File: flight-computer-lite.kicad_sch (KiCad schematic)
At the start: 23 parts, among them J1 USB_C_Receptacle_USB2.0_16P, J2 Micro_SD_Card_Det2, J3 Conn_01x02_Pin, J4 Conn_01x02_Pin, Q1 BSS138, U1 RP2040, U2 W25Q32JVZP, Y1 SiT1602BI-22-33E-12.000000E

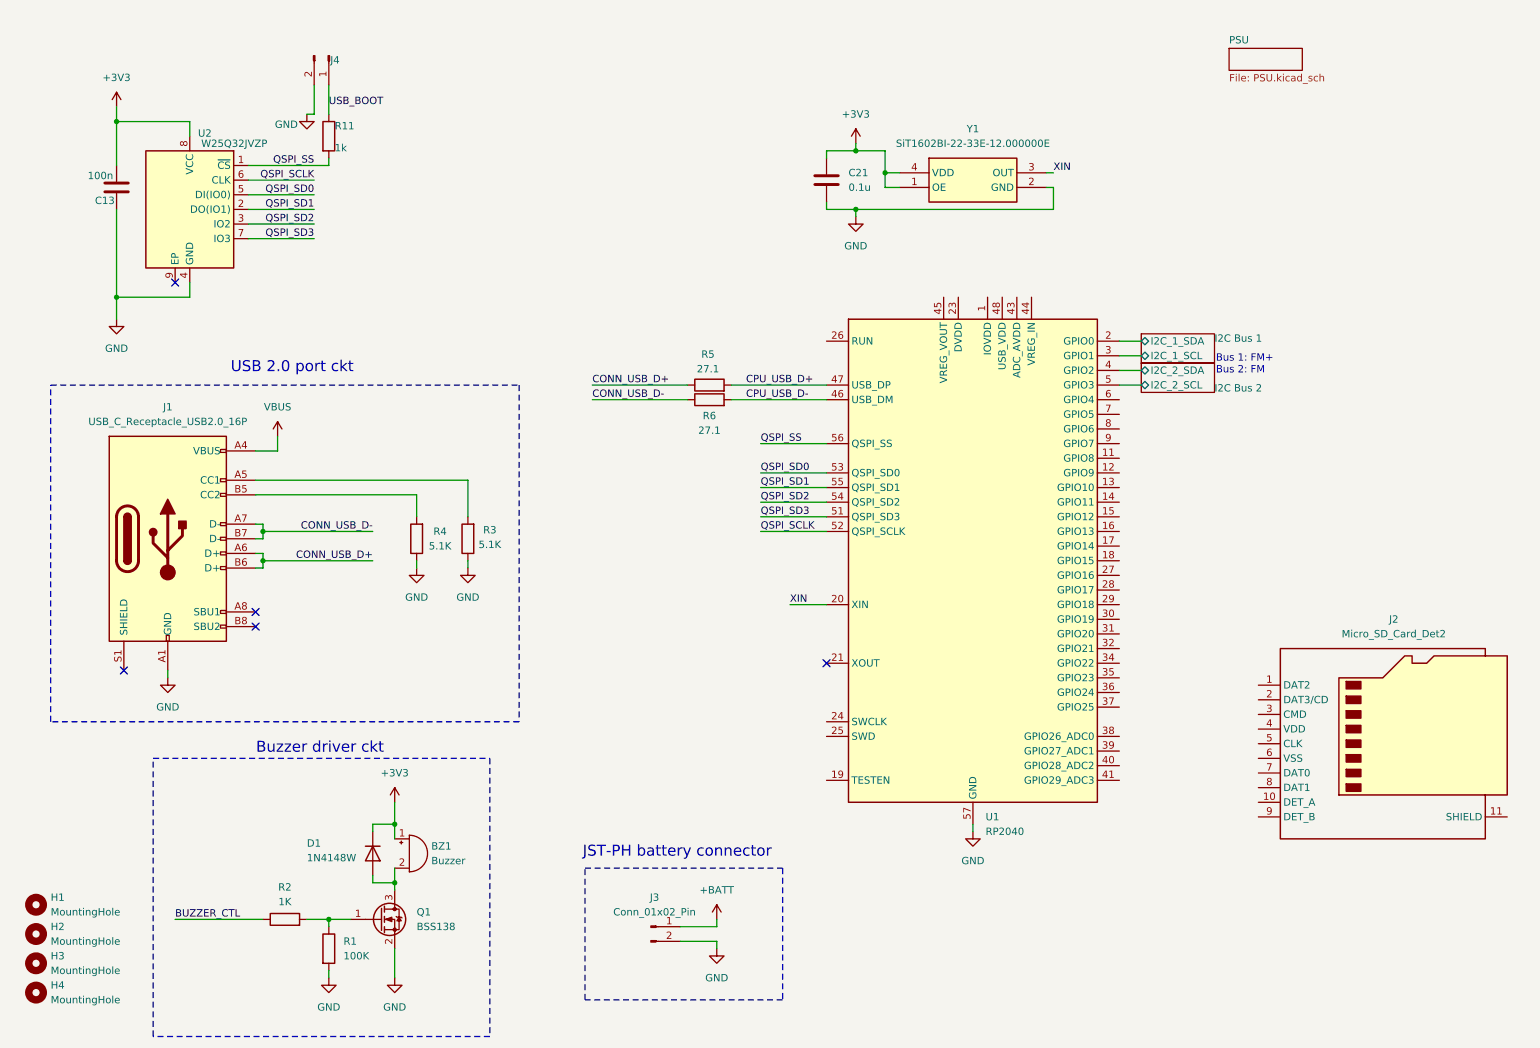
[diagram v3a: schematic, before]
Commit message: Added buttons, LEDs, TPs, and Miku
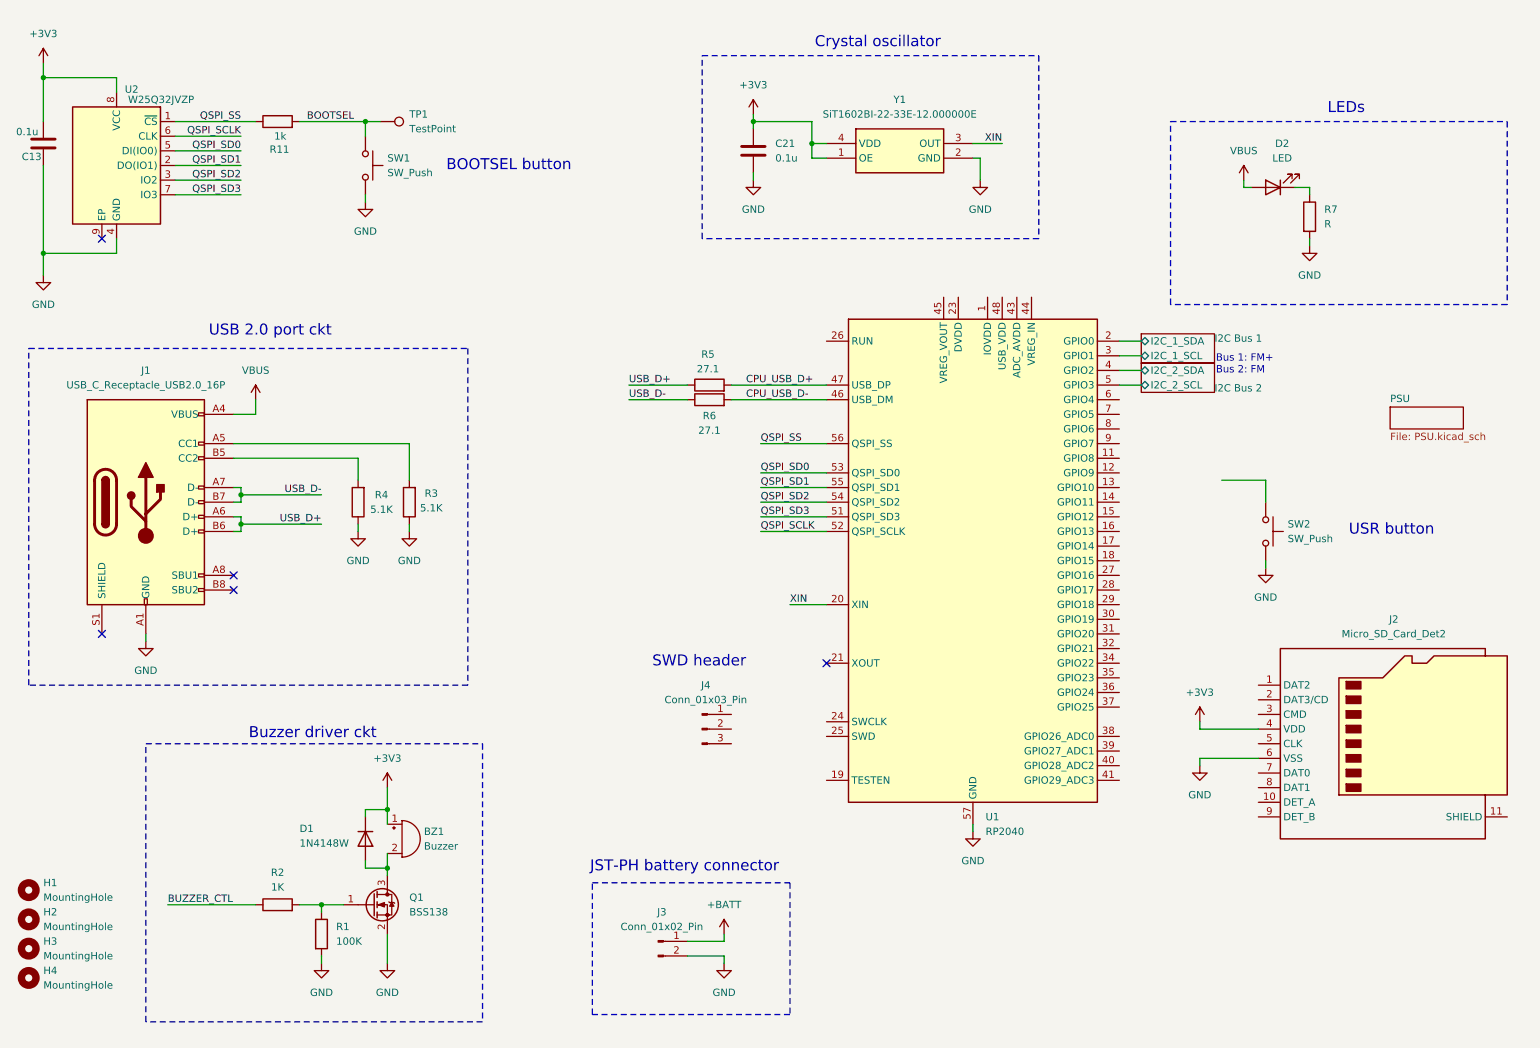
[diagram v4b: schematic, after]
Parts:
- removed J4: Conn_01x02_Pin, Connector_JST:JST_PH_S2B-PH-SM4-TB_1x02-1MP_P2.00mm_Horizontal, symbol Connector:Conn_01x02_Pin
- added D2: LED, LED_SMD:LED_0603_1608Metric, symbol Device:LED
- added J4: Conn_01x03_Pin, Connector_JST:JST_PH_B3B-PH-K_1x03_P2.00mm_Vertical, symbol Connector:Conn_01x03_Pin
- added R7: R, Resistor_SMD:R_0603_1608Metric, symbol Device:R
- added SW1, SW2: SW_Push, Button_Switch_SMD:SW_Push_1P1T_NO_Vertical_Wuerth_434133025816, symbol Switch:SW_Push
- added TP1: TestPoint, TestPoint:TestPoint_Pad_D1.0mm, symbol Connector:TestPoint
- C13: value 100n -> 0.1u
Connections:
- net USB_BOOT is gone; now on net QSPI_SS: R11.1
- net +3V3: now also J2.4 (VDD)
- net GND: now also J2.6 (VSS), R7.2, SW1.2, SW2.2
- net QSPI_SS: no longer R11.2
- net VBUS: now also D2.2 (A)
- net CONN_USB_D+ renamed USB_D+
- net CONN_USB_D- renamed USB_D-
- new net: D2.1 (K), R7.1
- new net BOOTSEL: R11.2, SW1.1, TP1.1
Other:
- note added: "BOOTSEL button"
- note added: "Crystal oscillator"
- note added: "LEDs"
- note added: "SWD header"
- note added: "USR button"
- moved on the sheet: BZ1, C13, C21, D1, H1, H2, H3, H4, J1, J3, Q1, R1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

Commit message: Added more decoupling caps
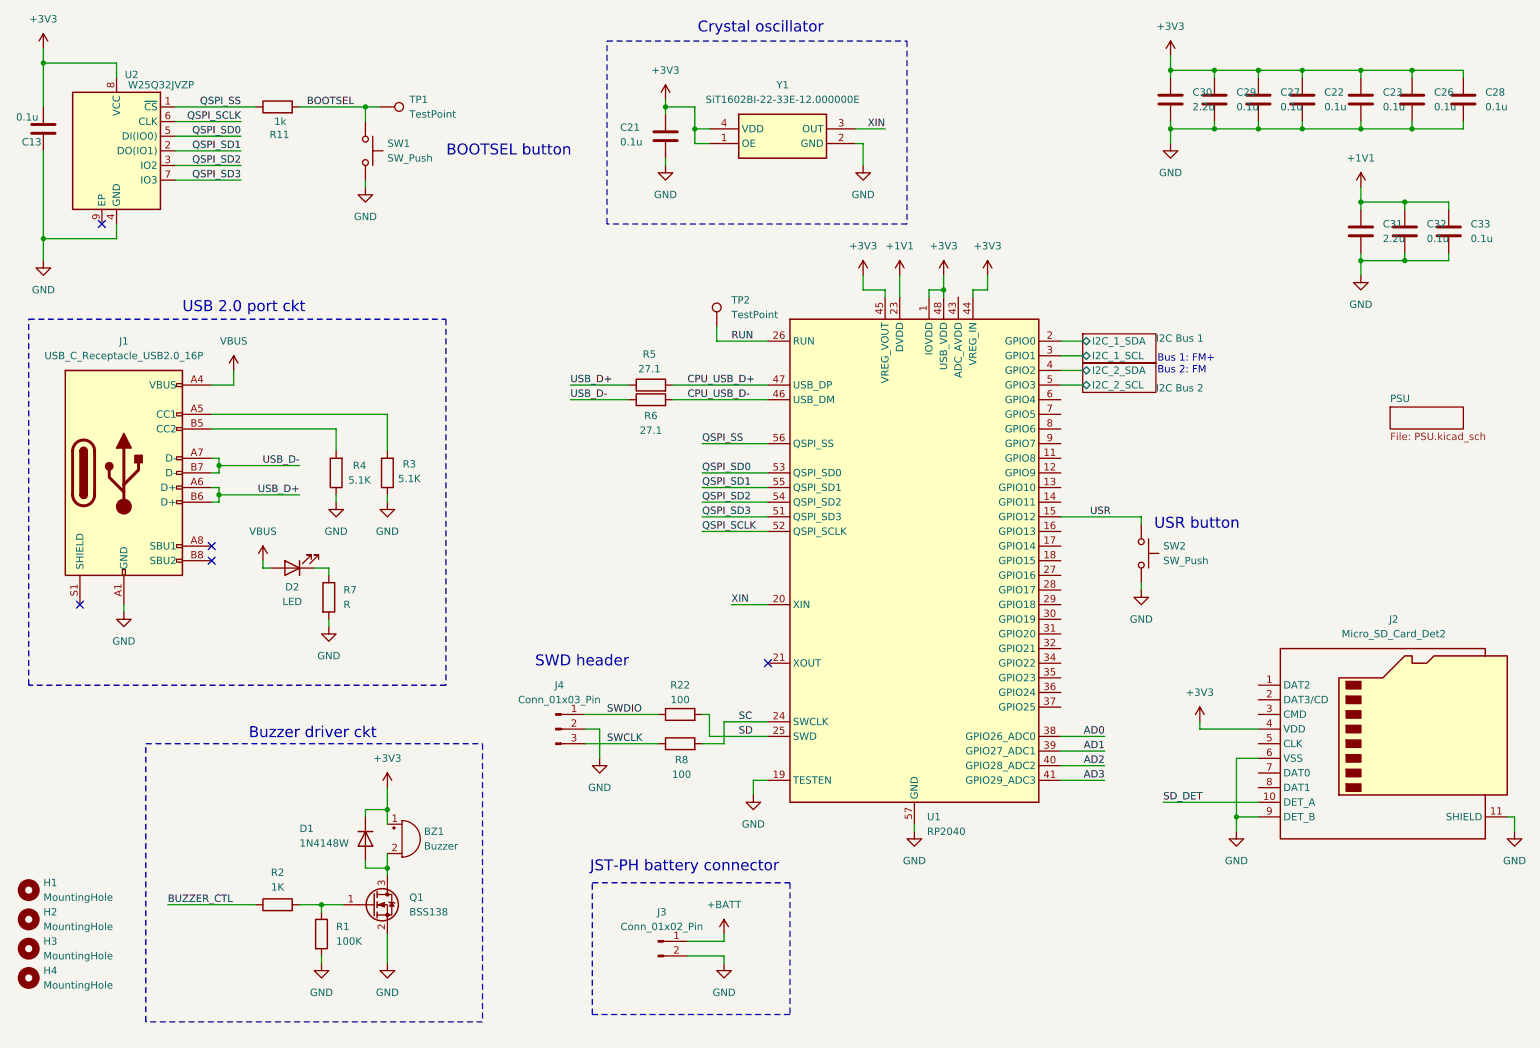
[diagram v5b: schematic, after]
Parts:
- added C22, C23, C26, C27, C28, C29, C32, C33: 0.1u, Capacitor_SMD:C_0603_1608Metric, symbol Device:C
- added C30, C31: 2.2u, Capacitor_SMD:C_0603_1608Metric, symbol Device:C
- added R22, R8: 100, Resistor_SMD:R_0603_1608Metric, symbol Device:R
- added TP2: TestPoint, TestPoint:TestPoint_Pad_D1.0mm, symbol Connector:TestPoint
- J4: footprint Connector_JST:JST_PH_B3B-PH-K_1x03_P2.00mm_Vertical -> Connector_JST:JST_SH_BM03B-SRSS-TB_1x03-1MP_P1.00mm_Vertical
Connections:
- net +3V3: now also U1.1 (IOVDD), U1.10 (IOVDD), U1.22 (IOVDD), U1.33 (IOVDD), U1.42 (IOVDD), U1.44 (VREG_IN), U1.45 (VREG_VOUT), U1.48 (USB_VDD), U1.49 (IOVDD), C22.1, C23.1, C26.1, C27.1, C28.1, C29.1, C30.1
- net GND: now also J2.11 (SHIELD), J2.9 (DET_B), J4.2 (Pin_2), U1.19 (TESTEN), C22.2, C23.2, C26.2, C27.2, C28.2, C29.2, C30.2, C31.2, C32.2, C33.2
- net USR: now reaches U1.15 (GPIO12)
- net USR: now also SW2.1
- net +1V1: now reaches U1.23 (DVDD), U1.50 (DVDD)
- net +1V1: now also C31.1, C32.1, C33.1
- net SC: now reaches U1.24 (SWCLK)
- net SC: now also R8.2
- net SD: now reaches U1.25 (SWD)
- net SD: now also R22.2
- net RUN: now reaches U1.26 (RUN)
- net RUN: now also TP2.1
- net AD0: now reaches U1.38 (GPIO26_ADC0)
- net AD1: now reaches U1.39 (GPIO27_ADC1)
- net AD2: now reaches U1.40 (GPIO28_ADC2)
- net AD3: now reaches U1.41 (GPIO29_ADC3)
- net SD_DET: now reaches J2.10 (DET_A)
- net SWDIO: now reaches J4.1 (Pin_1)
- net SWDIO: now also R22.1
- net SWCLK: now reaches J4.3 (Pin_3)
- net SWCLK: now also R8.1
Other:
- note removed: "LEDs"
- moved on the sheet: C13, C21, J1, R11, R3, R4, R5, R6, SW1, SW2, TP1, U1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

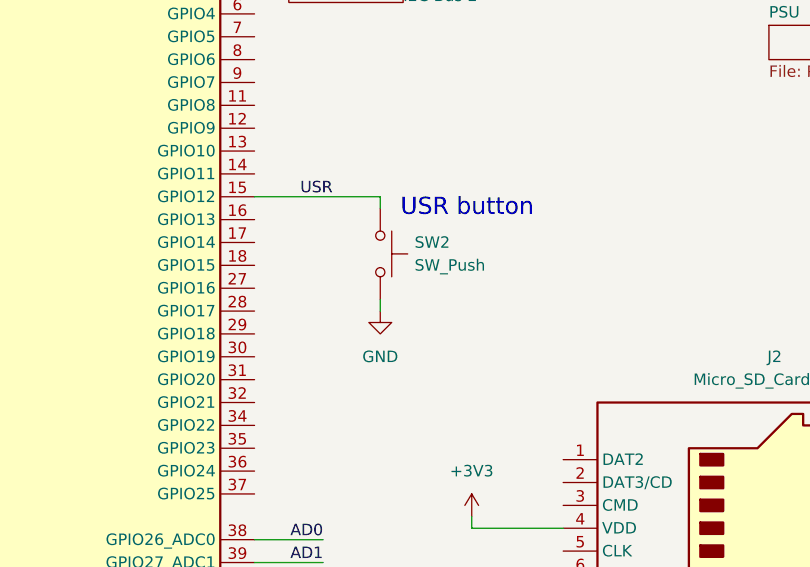
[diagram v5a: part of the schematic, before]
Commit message: Added more 3d models and rearranged layout
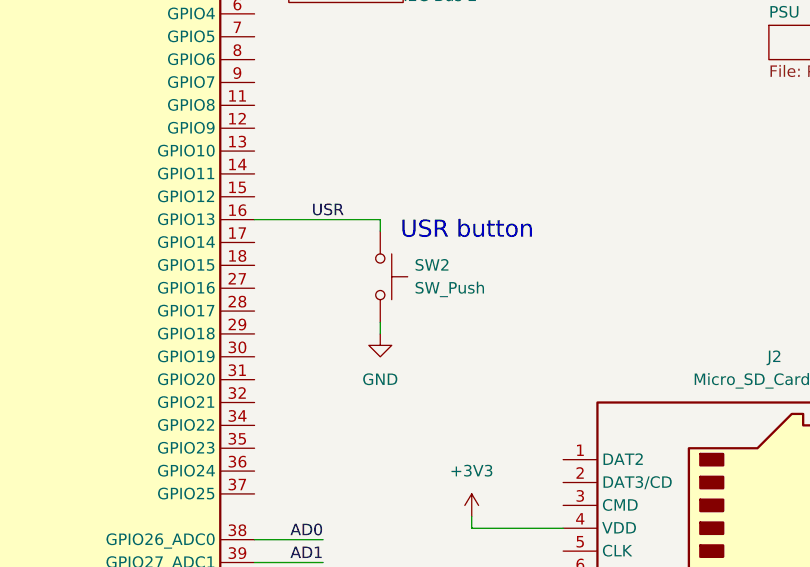
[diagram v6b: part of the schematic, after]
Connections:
- net USR: now also U1.16 (GPIO13); no longer U1.15 (GPIO12)
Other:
- moved on the sheet: SW2
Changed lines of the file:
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@@
 	(wire
 		(pts
-			(xy 213.36 104.14) (xy 213.36 102.87)
+			(xy 213.36 106.68) (xy 213.36 105.41)
 		)
 		(stroke
@@
 	(wire
 		(pts
-			(xy 199.39 102.87) (xy 213.36 102.87)
+			(xy 199.39 105.41) (xy 213.36 105.41)
 		)
 		(stroke
@@
 	(wire
 		(pts
-			(xy 213.36 114.3) (xy 213.36 115.57)
+			(xy 213.36 116.84) (xy 213.36 118.11)
 		)
 		(stroke
@@
 	(text "USR button"
 		(exclude_from_sim no)
-		(at 223.012 104.14 0)
+		(at 223.012 106.68 0)
 		(effects
 			(font
@@
 	)
 	(label "USR"
-		(at 204.47 102.87 0)
+		(at 205.74 105.41 0)
 		(fields_autoplaced yes)
 		(effects
@@
 	(symbol
 		(lib_id "Switch:SW_Push")
-		(at 213.36 109.22 270)
+		(at 213.36 111.76 270)
 		(unit 1)
 		(exclude_from_sim no)
@@
 		(fields_autoplaced yes)
 		(property "Reference" "SW2"
-			(at 217.17 107.9499 90)
+			(at 217.17 110.4899 90)
 			(effects
 				(font
@@
 		)
 		(property "Value" "SW_Push"
-			(at 217.17 110.4899 90)
+			(at 217.17 113.0299 90)
 			(effects
 				(font
@@
 		)
 		(property "Footprint" "Button_Switch_SMD:SW_Push_1P1T_NO_Vertical_Wuerth_434133025816"
-			(at 218.44 109.22 0)
+			(at 218.44 111.76 0)
 			(effects
 				(font
@@
 		)
 		(property "Datasheet" "~"
-			(at 218.44 109.22 0)
+			(at 218.44 111.76 0)
 			(effects
 				(font
@@
 		)
 		(property "Description" "Push button switch, generic, two pins"
-			(at 213.36 109.22 0)
+			(at 213.36 111.76 0)
 			(effects
 				(font
@@
 	(symbol
 		(lib_id "power:GND")
-		(at 213.36 115.57 0)
+		(at 213.36 118.11 0)
 		(unit 1)
 		(exclude_from_sim no)
@@
 		(fields_autoplaced yes)
 		(property "Reference" "#PWR030"
-			(at 213.36 121.92 0)
+			(at 213.36 124.46 0)
 			(effects
 				(font
@@
 		)
 		(property "Value" "GND"
-			(at 213.36 120.65 0)
+			(at 213.36 123.19 0)
 			(effects
 				(font
@@
 		)
 		(property "Footprint" ""
-			(at 213.36 115.57 0)
+			(at 213.36 118.11 0)
 			(effects
 				(font
@@
 		)
 		(property "Datasheet" ""
-			(at 213.36 115.57 0)
+			(at 213.36 118.11 0)
 			(effects
 				(font
@@
 		)
 		(property "Description" "Power symbol creates a global label with name \"GND\" , ground"
-			(at 213.36 115.57 0)
+			(at 213.36 118.11 0)
 			(effects
 				(font
